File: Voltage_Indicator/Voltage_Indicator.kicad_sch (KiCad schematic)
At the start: 20 parts, among them J1 PET-02-XX-X-VT-LC, K1 VORA1150-X017T, U1 LM393LVQDDFRQ1, U2 IPBT-102-H1-XX-S-RA

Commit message: Voltage Indicator All Files
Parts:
- CR1: footprint LED_AVAGO_HLMP_XX08_AVA -> Footprints:LED_AVAGO_HLMP_XX08_AVA
- CR2: footprint D2PAK_STM -> Footprints:D2PAK_STM
- J1: footprint Footprints:SAMTEC_PET-02-XX-X-VT-LC -> PES-02-01-X-RA-SD:SAMTEC_PES-02-01-X-RA-SD; symbol Symbols:PET-02-XX-X-VT-LC -> Symbols:PES-02-01-X-RA-SD; MAXIMUM_PACKAGE_HEIGHT 14.62mm -> 12mm
- K1: footprint SOP_VORA1150-X017T_VIS -> Footprints:SOP_VORA1150-X017T_VIS
- R1, R3, R4: footprint Resistor_SMD:R_0201_0603Metric -> SDM_MiscFootprint:R_1206_3216Metric
- R5: footprint Resistor_SMD:R_0201_0603Metric -> Resistor_SMD:R_1206_3216Metric
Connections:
- removed net 01: J1.01_1 (01), J1.01_2 (01), J1.01_3 (01), J1.01_4 (01), J1.01_5 (01), J1.01_6 (01), J1.01_7 (01), J1.01_8 (01), R1.1
- removed net 02: J1.02_1 (02), J1.02_2 (02), J1.02_3 (02), J1.02_4 (02), J1.02_5 (02), J1.02_6 (02), J1.02_7 (02), J1.02_8 (02), R6.2
- new net HV+: J1.P01_1 (P01), R1.1
- new net HV-: J1.P02_1 (P02), R6.2
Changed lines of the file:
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@@
 			)
 		)
-		(property "Footprint" "SOP_VORA1150-X017T_VIS"
+		(property "Footprint" "Footprints:SOP_VORA1150-X017T_VIS"
 			(at 203.2 90.17 0)
 			(effects
@@
 			)
 		)
-		(property "Footprint" "Resistor_SMD:R_0201_0603Metric"
+		(property "Footprint" "Resistor_SMD:R_1206_3216Metric"
 			(at 58.928 62.23 90)
 			(effects
@@
 			)
 		)
-		(property "Footprint" "Resistor_SMD:R_0201_0603Metric"
+		(property "Footprint" "SDM_MiscFootprint:R_1206_3216Metric"
 			(at 58.928 41.91 90)
 			(effects
@@
 			)
 		)
-		(property "Footprint" "Resistor_SMD:R_0201_0603Metric"
+		(property "Footprint" "SDM_MiscFootprint:R_1206_3216Metric"
 			(at 55.372 31.75 90)
 			(effects
@@
 			)
 		)
-		(property "Footprint" "LED_AVAGO_HLMP_XX08_AVA"
+		(property "Footprint" "Footprints:LED_AVAGO_HLMP_XX08_AVA"
 			(at 264.16 90.17 0)
 			(effects
@@
 	)
 	(symbol
-		(lib_id "Symbols:PET-02-XX-X-VT-LC")
+		(lib_id "Symbols:PES-02-01-X-RA-SD")
 		(at 38.1 40.64 0)
 		(unit 1)
@@
 			)
 		)
-		(property "Footprint" "Footprints:SAMTEC_PET-02-XX-X-VT-LC"
+		(property "Footprint" "PES-02-01-X-RA-SD:SAMTEC_PES-02-01-X-RA-SD"
 			(at 38.1 40.64 0)
 			(effects
@@
 			)
 		)
-		(property "MAXIMUM_PACKAGE_HEIGHT" "14.62mm"
+		(property "MAXIMUM_PACKAGE_HEIGHT" "12mm"
 			(at 38.1 40.64 0)
 			(effects
@@
 			)
 		)
-		(pin "01_7"
-		)
-		(pin "02_2"
-		)
-		(pin "02_1"
-		)
-		(pin "01_6"
-		)
-		(pin "01_5"
-		)
-		(pin "01_3"
-		)
-		(pin "01_8"
-		)
-		(pin "02_4"
-		)
-		(pin "02_6"
-		)
-		(pin "02_7"
-		)
-		(pin "02_8"
-		)
-		(pin "01_1"
-		)
-		(pin "01_2"
-		)
-		(pin "01_4"
-		)
-		(pin "02_3"
-		)
-		(pin "02_5"
+		(pin "P01_1"
+		)
+		(pin "P02_1"
 		)
 		(instances
@@
 			)
 		)
-		(property "Footprint" "D2PAK_STM"
+		(property "Footprint" "Footprints:D2PAK_STM"
 			(at 35.56 102.87 0)
 			(effects
@@
 			)
 		)
-		(property "Footprint" "Resistor_SMD:R_0201_0603Metric"
+		(property "Footprint" "SDM_MiscFootprint:R_1206_3216Metric"
 			(at 58.928 52.07 90)
 			(effects

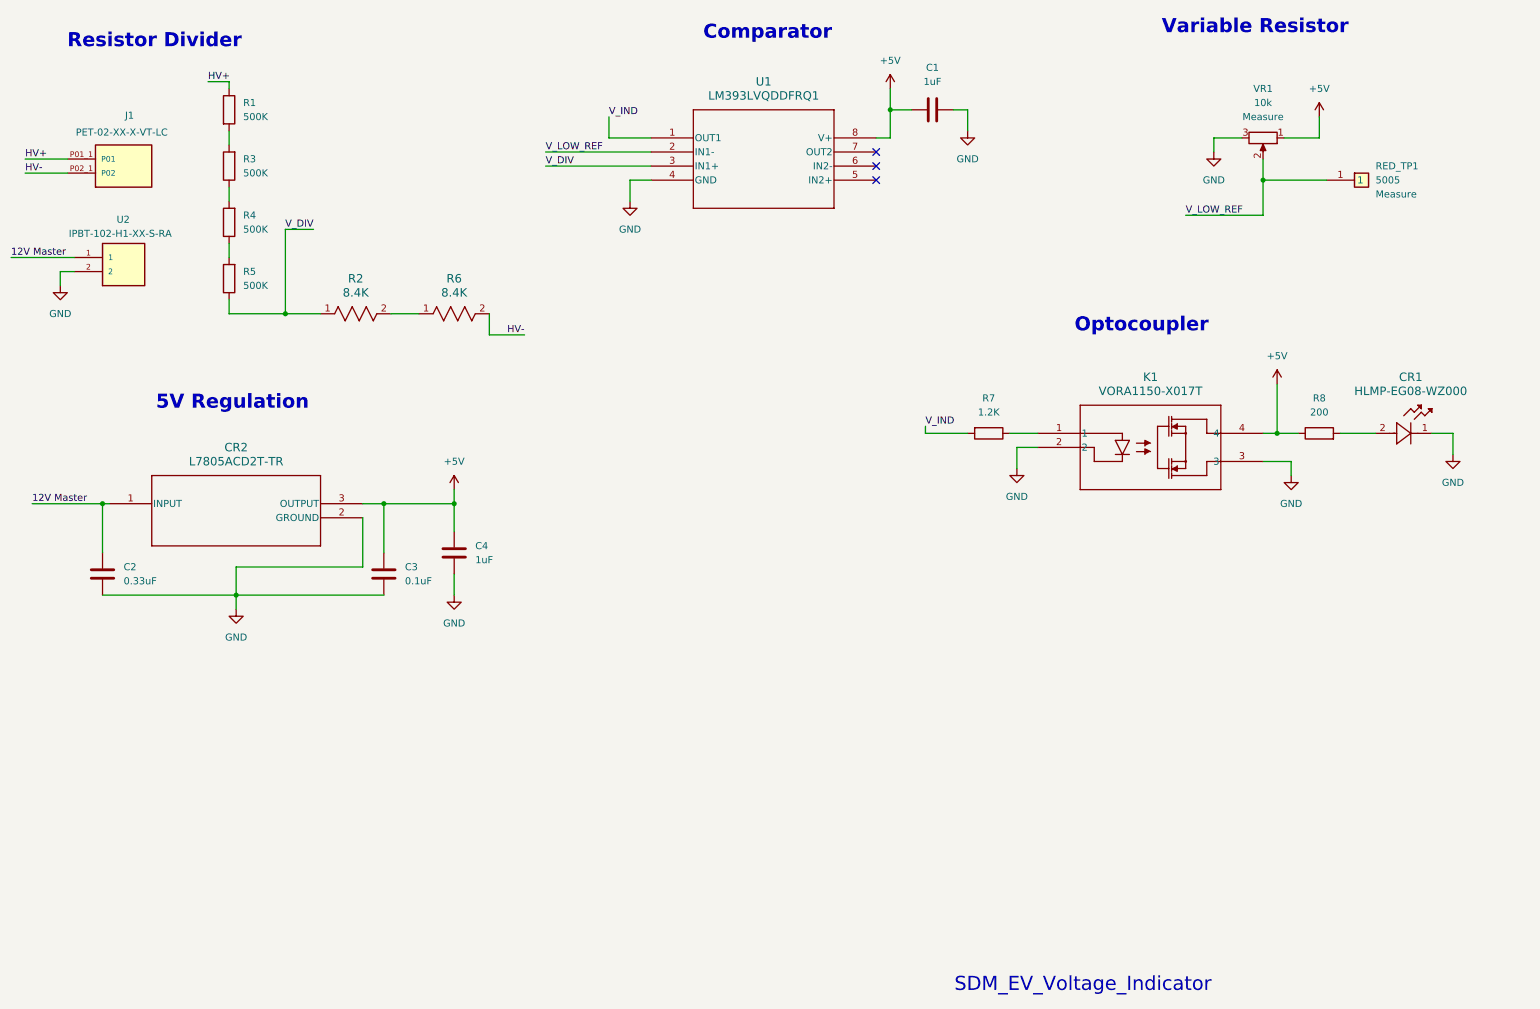
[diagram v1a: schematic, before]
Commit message: BSPD V1.2, Shutdown Circuit, Charging Shutdown Circuit, Voltage Indicator
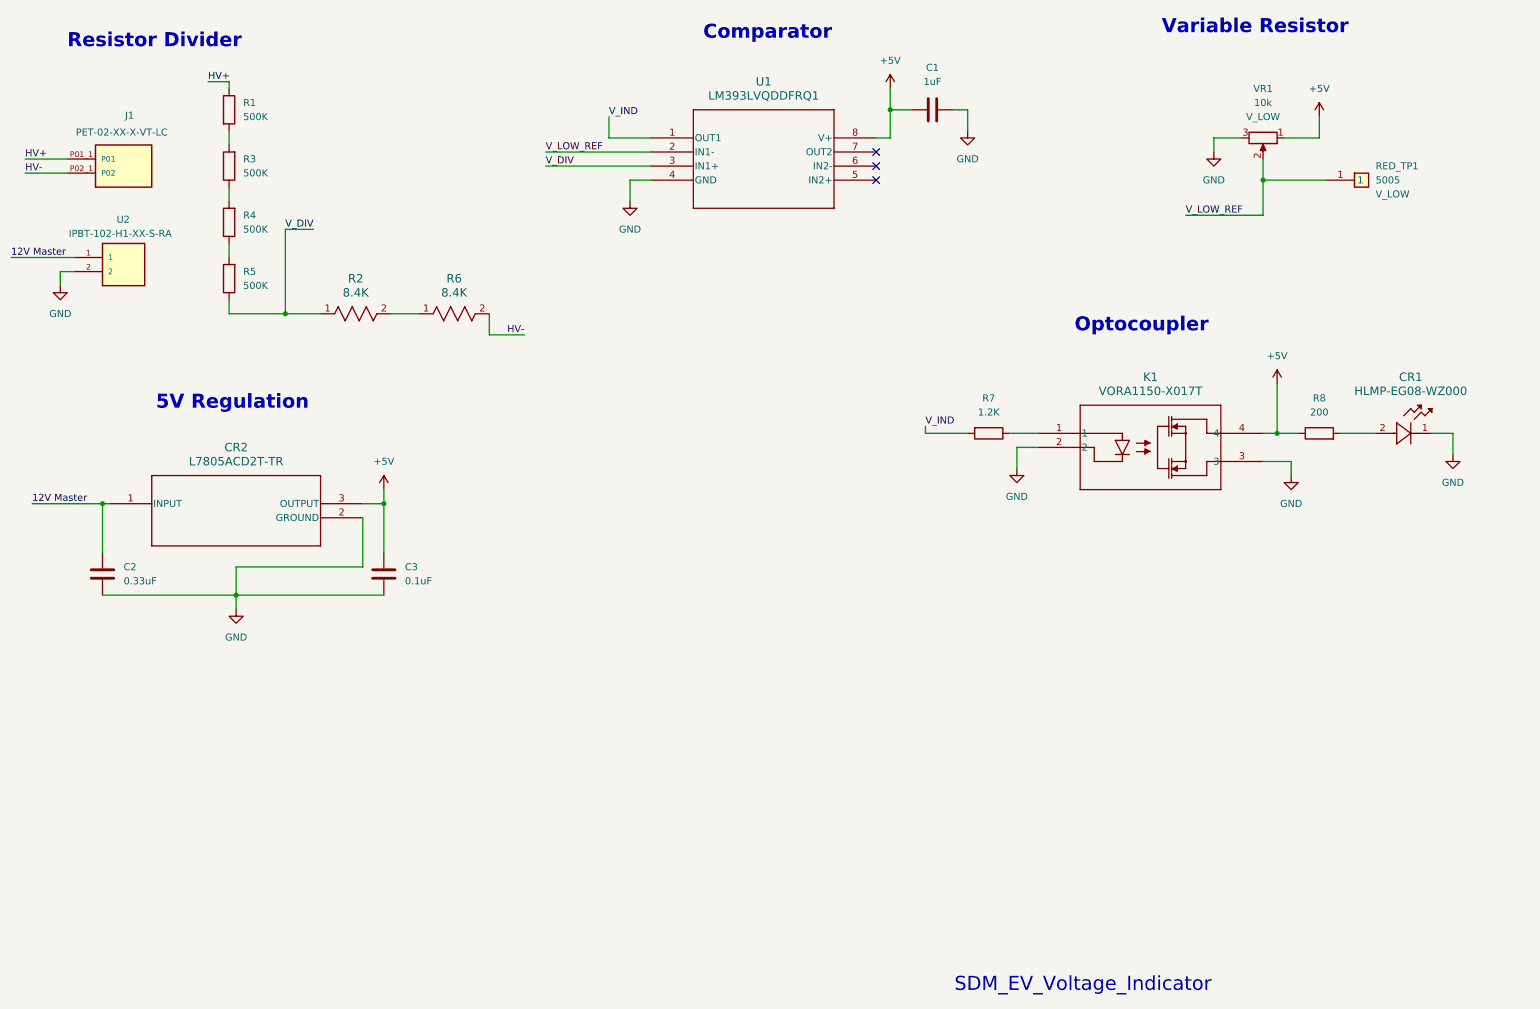
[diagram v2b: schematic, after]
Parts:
- removed C4: 1uF, Capacitor_SMD:C_0603_1608Metric, symbol Device:C
- J1: footprint PES-02-01-X-RA-SD:SAMTEC_PES-02-01-X-RA-SD -> Footprints:SAMTEC_PES-02-01-X-RA-SD
- RED_TP1, VR1: Measure Measure -> V_LOW
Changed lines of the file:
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@@
+	)
+	(junction
+		(at 85.09 102.87)
+		(diameter 0)
+		(color 0 0 0 0)
 	)
 	(junction
@@
 	)
 	(junction
-		(at 85.09 102.87)
-		(diameter 0)
-		(color 0 0 0 0)
-	)
-	(junction
 		(at 246.38 90.17)
-		(diameter 0)
-		(color 0 0 0 0)
-	)
-	(junction
-		(at 97.79 102.87)
 		(diameter 0)
 		(color 0 0 0 0)
@@
 	(wire
 		(pts
+			(xy 85.09 100.33) (xy 85.09 102.87)
+		)
+		(stroke
+			(width 0)
+			(type default)
+		)
+	)
+	(wire
+		(pts
 			(xy 234.95 36.83) (xy 234.95 39.37)
 		)
@@
 	(wire
 		(pts
-			(xy 97.79 100.33) (xy 97.79 102.87)
-		)
-		(stroke
-			(width 0)
-			(type default)
-		)
-	)
-	(wire
-		(pts
 			(xy 274.32 90.17) (xy 278.13 90.17)
 		)
@@
 	(wire
 		(pts
-			(xy 97.79 107.95) (xy 97.79 102.87)
-		)
-		(stroke
-			(width 0)
-			(type default)
-		)
-	)
-	(wire
-		(pts
 			(xy 257.81 90.17) (xy 264.16 90.17)
 		)
@@
 	(wire
 		(pts
-			(xy 97.79 115.57) (xy 97.79 119.38)
-		)
-		(stroke
-			(width 0)
-			(type default)
-		)
-	)
-	(wire
-		(pts
 			(xy 125.73 36.83) (xy 125.73 33.02)
 		)
@@
 		(pts
 			(xy 29.21 60.96) (xy 26.67 60.96)
-		)
-		(stroke
-			(width 0)
-			(type default)
-		)
-	)
-	(wire
-		(pts
-			(xy 85.09 102.87) (xy 97.79 102.87)
 		)
 		(stroke
@@
 	)
 	(symbol
-		(lib_id "Device:C")
-		(at 97.79 111.76 180)
-		(unit 1)
-		(exclude_from_sim no)
-		(in_bom yes)
-		(on_board yes)
-		(dnp no)
-		(fields_autoplaced yes)
-		(property "Reference" "C4"
-			(at 101.6 110.4899 0)
-			(effects
-				(font
-					(size 1.27 1.27)
-				)
-				(justify right)
-			)
-		)
-		(property "Value" "1uF"
-			(at 101.6 113.0299 0)
-			(effects
-				(font
-					(size 1.27 1.27)
-				)
-				(justify right)
-			)
-		)
-		(property "Footprint" "Capacitor_SMD:C_0603_1608Metric"
-			(at 96.8248 107.95 0)
-			(effects
-				(font
-					(size 1.27 1.27)
-				)
-				(hide yes)
-			)
-		)
-		(property "Datasheet" "~"
-			(at 97.79 111.76 0)
-			(effects
-				(font
-					(size 1.27 1.27)
-				)
-				(hide yes)
-			)
-		)
-		(property "Description" "Unpolarized capacitor"
-			(at 97.79 111.76 0)
-			(effects
-				(font
-					(size 1.27 1.27)
-				)
-				(hide yes)
-			)
-		)
-		(pin "1"
-		)
-		(pin "2"
-		)
-		(instances
-			(project "Voltage_Indicator"
-				(path "/5593afb4-6fc8-40c0-9307-9f2b2eba9183"
-					(reference "C4")
-					(unit 1)
-				)
-			)
-		)
-	)
-	(symbol
 		(lib_id "power:+5V")
 		(at 246.38 81.28 0)
@@
 		)
 		(instances
-			(project ""
+			(project "Voltage_Indicator"
 				(path "/5593afb4-6fc8-40c0-9307-9f2b2eba9183"
 					(reference "#PWR03")
@@
 		)
 		(instances
-			(project ""
+			(project "Voltage_Indicator"
 				(path "/5593afb4-6fc8-40c0-9307-9f2b2eba9183"
 					(reference "#PWR01")
@@
 		)
 		(instances
-			(project ""
+			(project "Voltage_Indicator"
 				(path "/5593afb4-6fc8-40c0-9307-9f2b2eba9183"
 					(reference "C1")
@@
 			)
 		)
-		(property "Measure" "Measure"
+		(property "Measure" "V_LOW"
 			(at 264.16 46.9899 0)
 			(effects
@@
 		)
 		(instances
-			(project ""
+			(project "Voltage_Indicator"
 				(path "/5593afb4-6fc8-40c0-9307-9f2b2eba9183"
 					(reference "RED_TP1")
@@
 		)
 		(instances
-			(project ""
+			(project "Voltage_Indicator"
 				(path "/5593afb4-6fc8-40c0-9307-9f2b2eba9183"
 					(reference "K1")
@@
 	)
 	(symbol
-		(lib_id "power:GND")
-		(at 97.79 119.38 0)
-		(unit 1)
-		(exclude_from_sim no)
-		(in_bom yes)
-		(on_board yes)
-		(dnp no)
-		(fields_autoplaced yes)
-		(property "Reference" "#PWR012"
-			(at 97.79 125.73 0)
-			(effects
-				(font
-					(size 1.27 1.27)
-				)
-				(hide yes)
-			)
-		)
-		(property "Value" "GND"
-			(at 97.79 124.46 0)
-			(effects
-				(font
-					(size 1.27 1.27)
-				)
-			)
-		)
-		(property "Footprint" ""
-			(at 97.79 119.38 0)
-			(effects
-				(font
-					(size 1.27 1.27)
-				)
-				(hide yes)
-			)
-		)
-		(property "Datasheet" ""
-			(at 97.79 119.38 0)
-			(effects
-				(font
-					(size 1.27 1.27)
-				)
-				(hide yes)
-			)
-		)
-		(property "Description" "Power symbol creates a global label with name \"GND\" , ground"
-			(at 97.79 119.38 0)
-			(effects
-				(font
-					(size 1.27 1.27)
-				)
-				(hide yes)
-			)
-		)
-		(pin "1"
-		)
-		(instances
-			(project "Voltage_Indicator"
-				(path "/5593afb4-6fc8-40c0-9307-9f2b2eba9183"
-					(reference "#PWR012")
-					(unit 1)
-				)
-			)
-		)
-	)
-	(symbol
 		(lib_id "Device:R")
 		(at 57.15 41.91 180)
@@
 		)
 		(instances
-			(project ""
+			(project "Voltage_Indicator"
 				(path "/5593afb4-6fc8-40c0-9307-9f2b2eba9183"
 					(reference "R1")
@@
 		)
 		(instances
-			(project ""
+			(project "Voltage_Indicator"
 				(path "/5593afb4-6fc8-40c0-9307-9f2b2eba9183"
 					(reference "#PWR04")
@@
 		)
 		(instances
-			(project ""
+			(project "Voltage_Indicator"
 				(path "/5593afb4-6fc8-40c0-9307-9f2b2eba9183"
 					(reference "#PWR02")
@@
 	(symbol
 		(lib_id "power:+5V")
-		(at 97.79 100.33 0)
+		(at 85.09 100.33 0)
 		(unit 1)
 		(exclude_from_sim no)
@@
 		(fields_autoplaced yes)
 		(property "Reference" "#PWR013"
-			(at 97.79 104.14 0)
+			(at 85.09 104.14 0)
 			(effects
 				(font
@@
 		)
 		(property "Value" "+5V"
-			(at 97.79 95.25 0)
+			(at 85.09 95.25 0)
 			(effects
 				(font
@@
 		)
 		(property "Footprint" ""
-			(at 97.79 100.33 0)
+			(at 85.09 100.33 0)
 			(effects
 				(font
@@
 		)
 		(property "Datasheet" ""
-			(at 97.79 100.33 0)
+			(at 85.09 100.33 0)
 			(effects
 				(font
@@
 		)
 		(property "Description" "Power symbol creates a global label with name \"+5V\""
-			(at 97.79 100.33 0)
+			(at 85.09 100.33 0)
 			(effects
 				(font
@@
 		)
 		(instances
-			(project ""
+			(project "Voltage_Indicator"
 				(path "/5593afb4-6fc8-40c0-9307-9f2b2eba9183"
 					(reference "#PWR013")
@@
 		)
 		(instances
-			(project ""
+			(project "Voltage_Indicator"
 				(path "/5593afb4-6fc8-40c0-9307-9f2b2eba9183"
 					(reference "U1")
@@
 			)
 		)
-		(property "Measure" "Measure"
+		(property "Measure" "V_LOW"
 			(at 243.84 33.02 0)
 			(effects
@@
 		)
 		(instances
-			(project ""
+			(project "Voltage_Indicator"
 				(path "/5593afb4-6fc8-40c0-9307-9f2b2eba9183"
 					(reference "VR1")
@@
 		)
 		(instances
-			(project ""
+			(project "Voltage_Indicator"
 				(path "/5593afb4-6fc8-40c0-9307-9f2b2eba9183"
 					(reference "R2")
@@
 		)
 		(instances
-			(project ""
+			(project "Voltage_Indicator"
 				(path "/5593afb4-6fc8-40c0-9307-9f2b2eba9183"
 					(reference "U2")
@@
 		)
 		(instances
-			(project ""
+			(project "Voltage_Indicator"
 				(path "/5593afb4-6fc8-40c0-9307-9f2b2eba9183"
 					(reference "CR1")
@@
 			)
 		)
-		(property "Footprint" "PES-02-01-X-RA-SD:SAMTEC_PES-02-01-X-RA-SD"
+		(property "Footprint" "Footprints:SAMTEC_PES-02-01-X-RA-SD"
 			(at 38.1 40.64 0)
 			(effects
@@
 		)
 		(instances
-			(project ""
+			(project "Voltage_Indicator"
 				(path "/5593afb4-6fc8-40c0-9307-9f2b2eba9183"
 					(reference "J1")
@@
 		)
 		(instances
-			(project ""
+			(project "Voltage_Indicator"
 				(path "/5593afb4-6fc8-40c0-9307-9f2b2eba9183"
 					(reference "CR2")

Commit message: BSPD, Shutdown/Charging Shutdown, & Voltage Indicator final changes
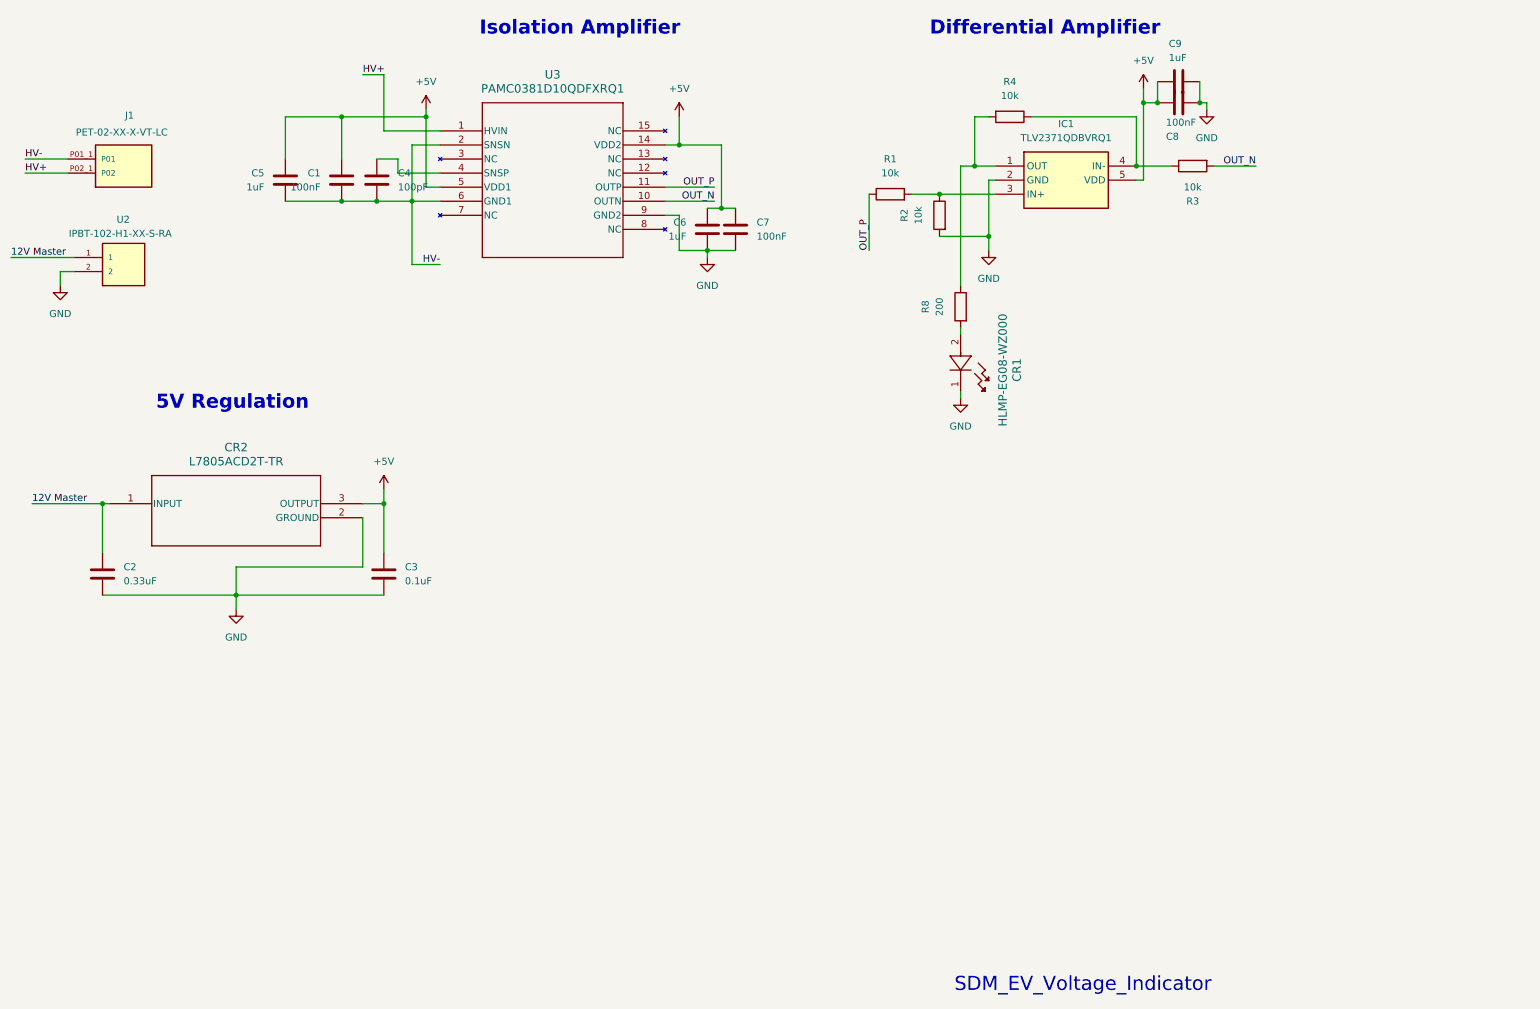
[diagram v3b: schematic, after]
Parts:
- removed K1: VORA1150-X017T, Footprints:SOP_VORA1150-X017T_VIS, symbol SDM_Parts:VORA1150-X017T
- removed R2, R6: 8.4K, Footprints:RES_ERA2A_PAN, symbol SDM_Parts:ERA-2ARB102X
- removed R5: 500K, Resistor_SMD:R_1206_3216Metric, symbol Device:R
- removed R7: 1.2K, Resistor_SMD:R_0201_0603Metric, symbol Device:R
- removed RED_TP1: 5005, Footprints:5005, symbol Symbols:5005
- removed U1: LM393LVQDDFRQ1, Footprints:SOT-23-THIN8_DDF_TEX, symbol SDM_Parts:LM393LVQDDFRQ1
- removed VR1: 10k, Footprints:3386P1103TLF, symbol Symbols:3386P-1-103TLF
- added C4: 100pF, Capacitor_SMD:C_0603_1608Metric, symbol Device:C
- added C5, C6, C9: 1uF, Capacitor_SMD:C_0603_1608Metric, symbol Device:C
- added C7, C8: 100nF, Capacitor_SMD:C_0603_1608Metric, symbol Device:C
- added IC1: TLV2371QDBVRQ1, Footprints:SOT95P280X145-5N, symbol Symbols:TLV2371QDBVRQ1
- added R2: 10k, Resistor_SMD:R_0603_1608Metric, symbol Device:R
- added U3: PAMC0381D10QDFXRQ1, Footprints:SSOP15_DFX_TEX, symbol Symbols:PAMC0381D10QDFXRQ1
- C1: value 1uF -> 100nF
- CR2: footprint Footprints:D2PAK_STM -> Footprints:L7805ACD2TTR
- R1, R3, R4: value 500K -> 10k; footprint SDM_MiscFootprint:R_1206_3216Metric -> Resistor_SMD:R_0603_1608Metric
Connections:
- net +5V: now also C1.2, C5.2, C6.2, C7.2, C8.2, C9.2, IC1.5 (VDD), U3.14 (VDD2), U3.5 (VDD1); no longer C1.1, R8.1
- net GND: now also C6.1, C7.1, C8.1, C9.1, IC1.2 (GND), R2.2, U3.9 (GND2); no longer C1.2
- net HV+: now also J1.P02_1 (P02), U3.1 (HVIN); no longer J1.P01_1 (P01), R1.1
- net HV-: now also C1.1, J1.P01_1 (P01), C4.1, C5.1, U3.2 (SNSN), U3.6 (GND1); no longer J1.P02_1 (P02)
- net at R4.1: now also R3.1, IC1.4 (IN-)
- net at R4.2: now also R8.1, IC1.1 (OUT); no longer R3.1
- net at R1.2: now also IC1.3 (IN+), R2.1; no longer R3.2
- new net: C4.2, U3.4 (SNSP)
- new net OUT_N: R3.2, U3.10 (OUTN)
- new net OUT_P: R1.1, U3.11 (OUTP)
- no-connect marks 3 -> 0
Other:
- note added: "Differential Amplifier"
- note added: "Isolation Amplifier"
- note removed: "Comparator"
- note removed: "Optocoupler"
- note removed: "Resistor Divider"
- note removed: "Variable Resistor"
- moved on the sheet: CR1, R8
